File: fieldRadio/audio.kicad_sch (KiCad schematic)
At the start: 49 parts, among them Q1 MMBT3906, Q2 MMBT3904, Q3 PZT2222A, Q4 PZT2907A

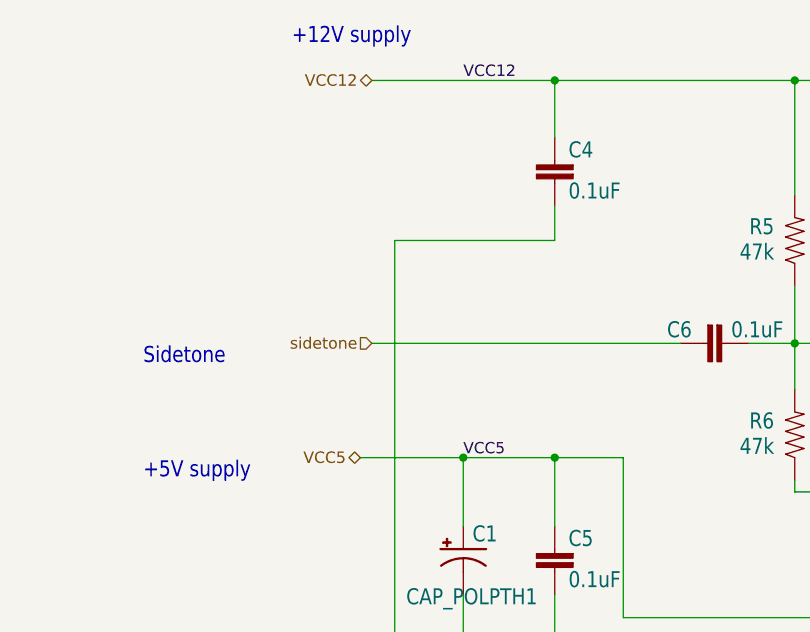
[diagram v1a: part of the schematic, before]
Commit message: Updating field radio
Continued schematic work on field radio
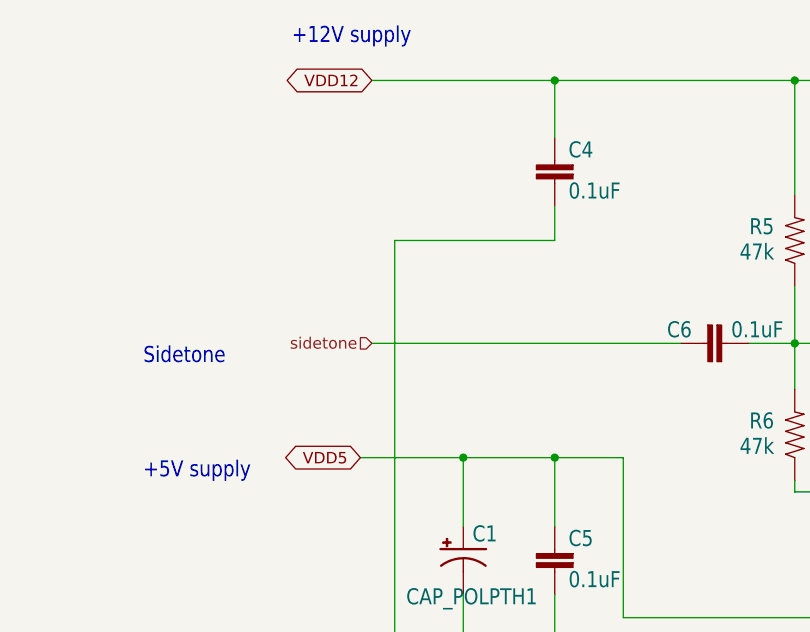
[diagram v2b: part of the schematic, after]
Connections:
- net VCC12 renamed VDD12
- net VCC5 renamed VDD5
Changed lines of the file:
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@@
     (effects (font (size 1.2446 1.2446)) (justify left bottom))
-  )
-  (label "VCC12" (at 91.44 36.83 0) (fields_autoplaced)
-    (effects (font (size 1.27 1.27)) (justify left bottom))
   )
   (label "MUTE" (at 125.73 139.7 0) (fields_autoplaced)
@@
     (effects (font (size 1.2446 1.2446)) (justify left bottom))
   )
-  (label "VCC5" (at 91.44 78.74 0) (fields_autoplaced)
-    (effects (font (size 1.2446 1.2446)) (justify left bottom))
+  (global_label "VDD12" (shape bidirectional) (at 81.28 36.83 180) (fields_autoplaced)
+    (effects (font (size 1.27 1.27)) (justify right))
+    (property "Intersheetrefs" "${INTERSHEET_REFS}" (at 71.6774 36.83 0)
+      (effects (font (size 1.27 1.27)) (justify right))
+    )
+  )
+  (global_label "VDD5" (shape bidirectional) (at 80.01 78.74 180) (fields_autoplaced)
+    (effects (font (size 1.27 1.27)) (justify right))
+    (property "Intersheetrefs" "${INTERSHEET_REFS}" (at 71.3963 78.74 0)
+      (effects (font (size 1.27 1.27)) (justify right))
+    )
   )
   (hierarchical_label "audio_narrow" (shape input) (at 81.28 116.84 180) (fields_autoplaced)
@@
     (effects (font (size 1.27 1.27)) (justify right))
   )
-  (hierarchical_label "VCC12" (shape bidirectional) (at 81.28 36.83 180) (fields_autoplaced)
-    (effects (font (size 1.27 1.27)) (justify right))
-  )
   (hierarchical_label "sidetone" (shape input) (at 81.28 66.04 180) (fields_autoplaced)
     (effects (font (size 1.27 1.27)) (justify right))
   )
-  (hierarchical_label "VCC5" (shape bidirectional) (at 80.01 78.74 180) (fields_autoplaced)
-    (effects (font (size 1.27 1.27)) (justify right))
-  )

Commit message: More schematic dev.
More schematic development
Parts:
- renumbered C1 to C66, C2 to C67, C3 to C68, C4 to C69, C5 to C70, C6 to C71, C7 to C72, C9 to C73, C10 to C74, C11 to C75, C8 to C76, C17 to C77, C13 to C78, C14 to C79, C15 to C80, C18 to C81, C19 to C82, C12 to C83, C16 to C84, D1 to D20, D2 to D21, JP11 to JP2, Q1 to Q14, Q2 to Q15, Q3 to Q16, Q4 to Q17, R1 to R64, R2 to R65, R3 to R66, R5 to R67, R6 to R68, R7 to R69, R9 to R70, R10 to R71, R11 to R72, R12 to R73, R13 to R74, R14 to R75, R15 to R76, R16 to R77, R17 to R78, R4 to R79, R8 to R80, R18 to R81, R19 to R82, R20 to R83, U$1 to U$2, U$2 to U$3

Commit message: Update Connectors
Changed to PCB mount connectors for back panel
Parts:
- removed C83: 4.7uF, Capacitor_THT:CP_Radial_D6.3mm_P2.50mm, symbol audioModule2-eagle-import:CAP_POLPTH1
- removed D20, D21: 1N4148, Diode_THT:D_DO-35_SOD27_P7.62mm_Horizontal, symbol Diode:1N4148
- removed JP2: M03PTH, Connector_PinHeader_2.54mm:PinHeader_1x03_P2.54mm_Vertical, symbol audioModule2-eagle-import:M03PTH
- removed Q14: MMBT3906, Package_TO_SOT_SMD:SOT-23, symbol Device:Q_PNP_BEC
- removed Q15: MMBT3904, Package_TO_SOT_SMD:SOT-23, symbol Device:Q_NPN_BEC
- removed Q16: PZT2222A, Package_TO_SOT_SMD:SOT-223, symbol Device:Q_NPN_BCEC
- removed Q17: PZT2907A, Package_TO_SOT_SMD:SOT-223, symbol Device:Q_PNP_BCEC
- removed R77: 14.3k, Resistor_SMD:R_0603_1608Metric_Pad0.98x0.95mm_HandSolder, symbol Device:R_US
- removed R78: 75, Resistor_SMD:R_0603_1608Metric_Pad0.98x0.95mm_HandSolder, symbol Device:R_US
- removed R79, R80: 47, Resistor_SMD:R_0805_2012Metric_Pad1.20x1.40mm_HandSolder, symbol Device:R_US
- removed R81, R82: 1, Resistor_SMD:R_0805_2012Metric_Pad1.20x1.40mm_HandSolder, symbol Device:R_US
- removed R83: 1k, Resistor_SMD:R_0603_1608Metric_Pad0.98x0.95mm_HandSolder, symbol audioModule2-eagle-import:RESISTOR0603-RES
- removed RV2: 2K, Potentiometer_THT:Potentiometer_Bourns_3296W_Vertical, symbol Device:R_Potentiometer_US
- added C37: 47nF, Capacitor_SMD:C_0603_1608Metric_Pad1.08x0.95mm_HandSolder, symbol audioModule2-eagle-import:CAP0603-CAP
- added C38: 100uF, Capacitor_THT:CP_Radial_D6.3mm_P2.50mm, symbol audioModule2-eagle-import:CAP_POLPTH1
- added C39: DNS, Capacitor_THT:CP_Radial_D6.3mm_P2.50mm, symbol audioModule2-eagle-import:CAP_POLPTH1
- added C40: DNS, Capacitor_SMD:C_0603_1608Metric_Pad1.08x0.95mm_HandSolder, symbol audioModule2-eagle-import:CAP0603-CAP
- added J3: Conn_01x03, symbol Connector_Generic:Conn_01x03
- added R27: 10, Resistor_SMD:R_0603_1608Metric_Pad0.98x0.95mm_HandSolder, symbol audioModule2-eagle-import:RESISTOR0603-RES
- added R28: DNS, Resistor_SMD:R_0603_1608Metric_Pad0.98x0.95mm_HandSolder, symbol audioModule2-eagle-import:RESISTOR0603-RES
- added U1: LM386, symbol Amplifier_Audio:LM386
- R76: value 0 -> 33k
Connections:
- net GND: now also C40.1, J3.3 (Pin_3), R27.2, U1.2 (-), U1.4 (GND)
- net VDD12: now also U1.6 (V+)
- net audio_out: now also C38.2 (-); no longer C84.2 (-)
- net at C84.1 (+): now also R76.2, U$3.7 (OUT)
- new net: R28.1, U1.1 (GAIN)
- new net: J3.2 (Pin_2), U1.3 (+)
- new net: C37.2, C38.1 (+), U1.5
- new net: C40.2, U1.7 (BYPASS)
- new net: C39.2 (-), U1.8 (GAIN)
- new net: C39.1 (+), R28.2
- new net: C37.1, R27.1
- new net: C84.2 (-), J3.1 (Pin_1)
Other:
- note removed: "100K ohms pot"
- moved on the sheet: C84

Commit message: Clean Up
Schematic clean up in prep for layout
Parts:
- J10: renamed from J3; footprint (none) -> Connector_PinHeader_2.54mm:PinHeader_1x03_P2.54mm_Vertical
- U6: renamed from U1; footprint (none) -> Package_DIP:DIP-8_W10.16mm_LongPads
- renumbered C66 to C71, C67 to C72, C68 to C73, C69 to C74, C70 to C75, C71 to C76, C72 to C77, C73 to C78, C74 to C79, C75 to C80, C76 to C81, C77 to C82, C78 to C83, C79 to C84, C80 to C85, C81 to C86, C82 to C87, C84 to C88, C39 to C89, C40 to C90, C37 to C91, C38 to C92, R64 to R63, R65 to R64, R66 to R65, R67 to R66, R68 to R67, R69 to R68, R70 to R69, R71 to R70, R72 to R71, R73 to R72, R74 to R73, R75 to R74, R76 to R75, R28 to R76, R27 to R77
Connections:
- net sidetone renamed SIDETONE

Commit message: Placement Update
LPF and TR Switch placed
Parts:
- U$2: footprint audioModule2:MSOP10 -> Package_SO:VSSOP-10_3x3mm_P0.5mm
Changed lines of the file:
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@@
       (effects (font (size 1.778 1.5113)) (justify left bottom))
     )
-    (property "Footprint" "audioModule2:MSOP10" (at 139.7 142.24 0)
+    (property "Footprint" "Package_SO:VSSOP-10_3x3mm_P0.5mm" (at 139.7 142.24 0)
       (effects (font (size 1.27 1.27)) hide)
     )

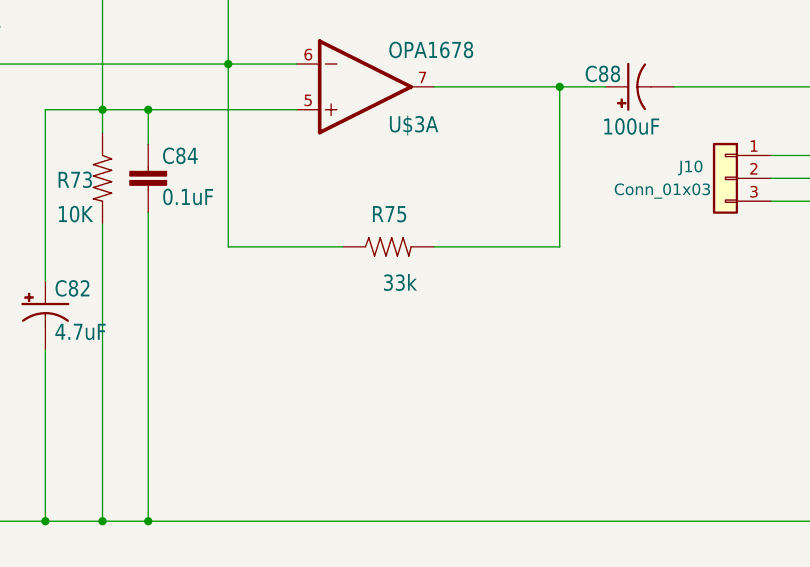
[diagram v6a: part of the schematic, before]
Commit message: Placement Refinement 1
Ungrouping blocks and optimizing placement
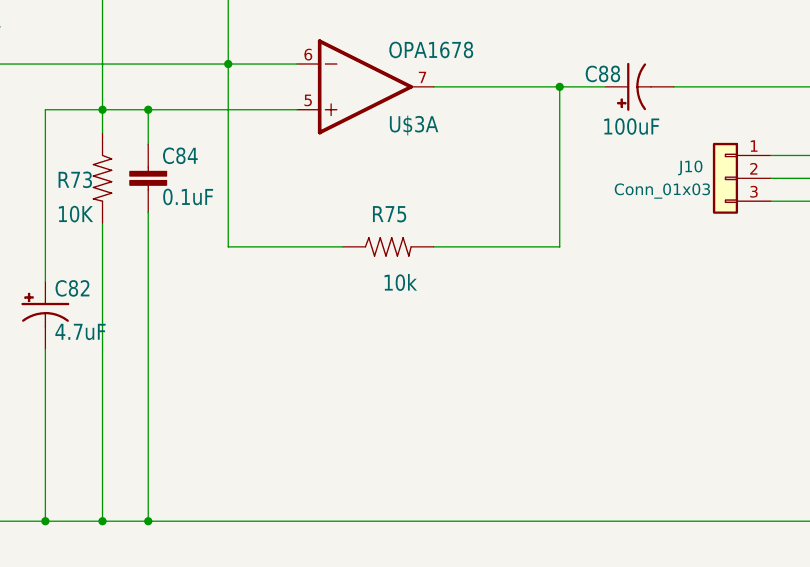
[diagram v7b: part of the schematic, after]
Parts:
- R75: value 33k -> 10k
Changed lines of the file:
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@@
       (effects (font (size 1.778 1.5113)) (justify left bottom))
     )
-    (property "Value" "33k" (at 227.965 152.4 0)
+    (property "Value" "10k" (at 227.965 152.4 0)
       (effects (font (size 1.778 1.5113)) (justify left bottom))
     )
@@
       (effects (font (size 1.27 1.27)) hide)
     )
+    (property "Mouser Part Number" "" (at 228.6 147.32 0)
+      (effects (font (size 1.27 1.27)) hide)
+    )
